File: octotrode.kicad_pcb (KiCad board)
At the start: 2 copper layers, 76 x 76 mm, 28 parts, among them J1 Conn_01x01, J2 Conn_01x01, J3 Conn_01x01, J4 Conn_01x01, J5 Conn_01x01, J6 Conn_01x01, Q1 Q_Photo_NPN, Q2 Q_Photo_NPN, Q3 Q_Photo_NPN, Q4 Q_Photo_NPN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

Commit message: add reverse voltage protection
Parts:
- added D5: D, Diode_SMD:D_SOD-123F, F.Cu at (188.5, 139.5)
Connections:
- J5 pad 1: +5V -> Net-(D5-Pad2)
- U1 pad 10: Net-(U1-Pad10) -> (no net)
- U1 pad 12: Net-(U1-Pad12) -> (no net)
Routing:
- net Net-(D5-Pad2): track 0.00 -> 10.4 mm

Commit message: correct LED orientation
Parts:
- moved D1 2.54 mm to (156.3, 146.0), turned to 180 degrees
- moved D3 2.54 mm to (163.7, 94.0), turned to 0 degrees
- moved D2 2.54 mm to (134.0, 116.3), turned to 90 degrees
- moved D4 2.54 mm to (186.0, 123.7), turned to 270 degrees
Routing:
- net Net-(D3-Pad2): track 3.43 -> 4.56 mm
- net Net-(D1-Pad2): track 3.43 -> 4.56 mm
- net Net-(D4-Pad2): track 3.43 -> 4.56 mm
- net Net-(D2-Pad2): track 3.43 -> 4.56 mm

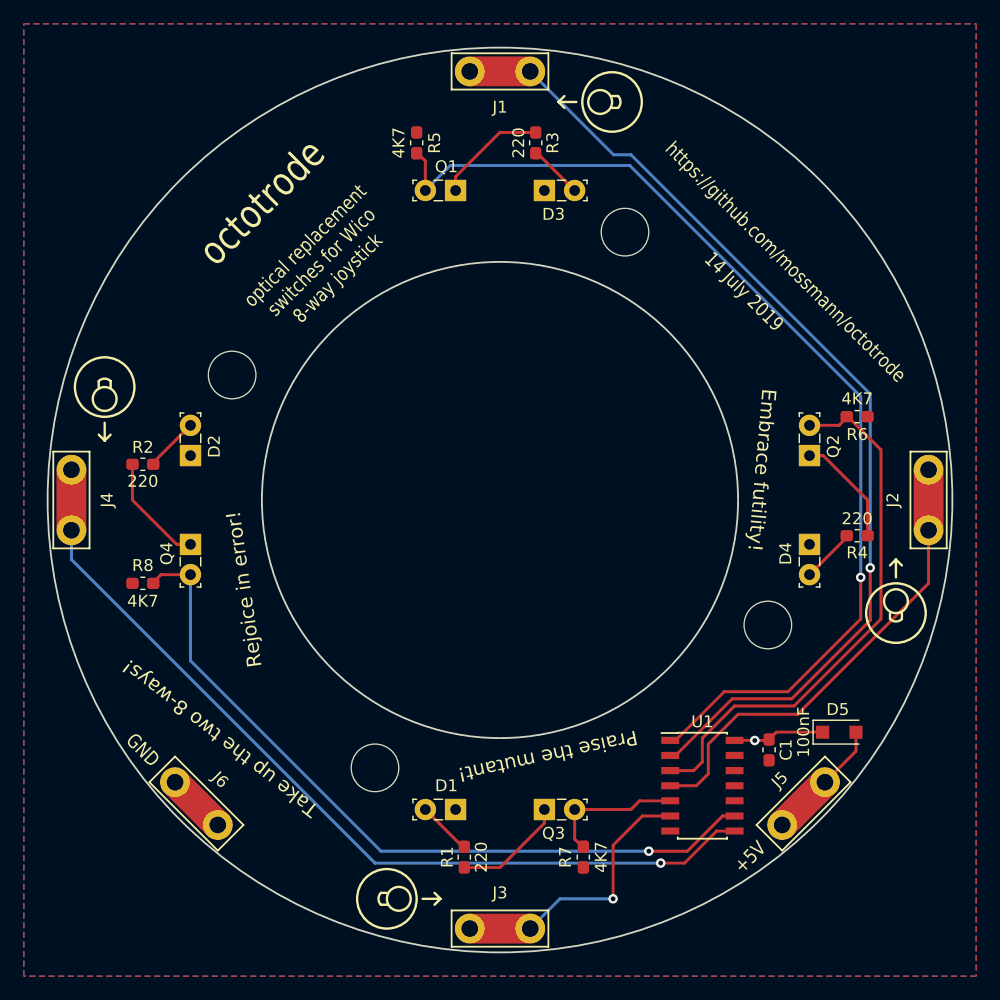
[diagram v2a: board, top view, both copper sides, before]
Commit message: widen optics position, shrink board
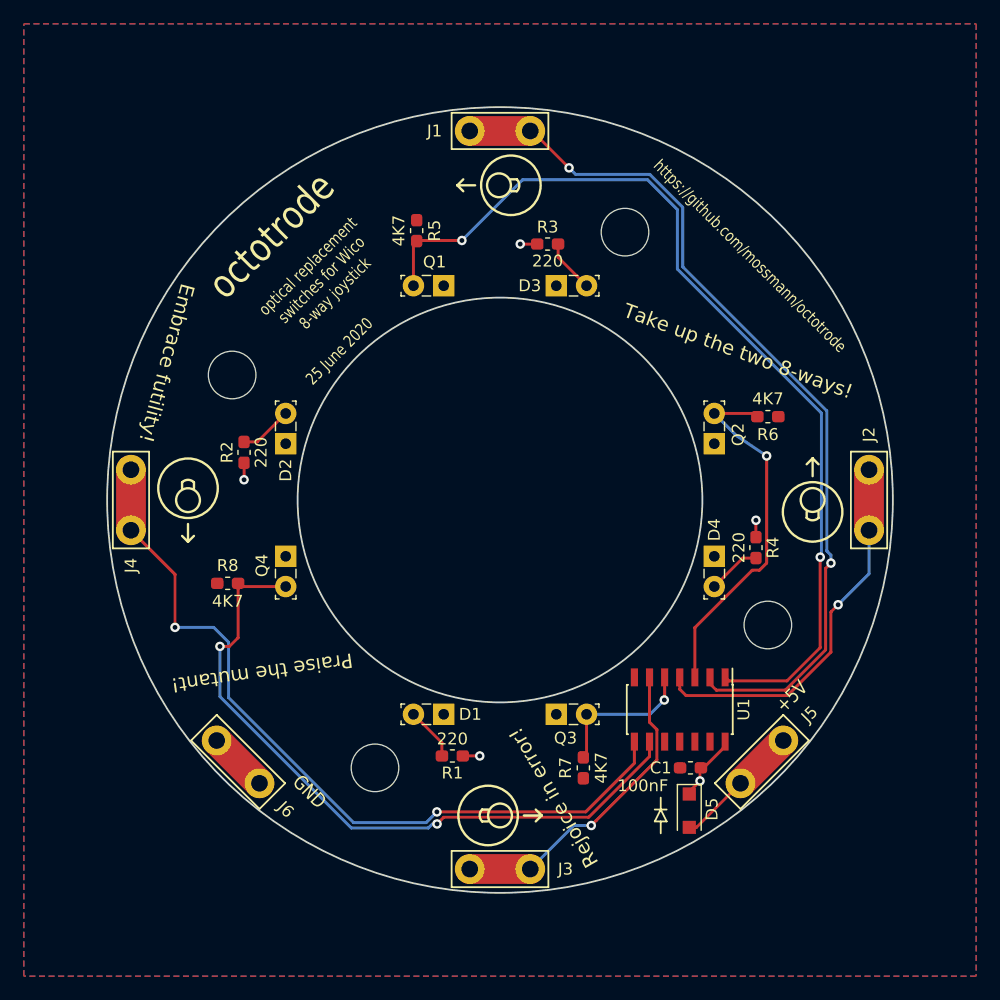
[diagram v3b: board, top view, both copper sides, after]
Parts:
- moved D5 14.2 mm to (175.9, 146.1), turned to 270 degrees
- moved R1 8.56 mm to (156.0, 141.5), turned to 180 degrees
- moved R2 8.56 mm to (138.5, 116.0), turned to 90 degrees
- moved R3 8.56 mm to (164.0, 98.5), turned to 0 degrees
- moved R4 8.56 mm to (181.5, 124.0), turned to 270 degrees
- moved D1 8.06 mm to (155.3, 138.0)
- moved D2 8.06 mm to (142.0, 115.3)
- moved D3 8.06 mm to (164.7, 102.0)
- moved D4 8.06 mm to (178.0, 124.7)
- moved Q1 8.06 mm to (155.3, 102.0)
- moved Q2 8.06 mm to (178.0, 115.3)
- moved Q3 8.06 mm to (164.7, 138.0)
- moved Q4 8.06 mm to (142.0, 124.7)
- moved R6 7.50 mm to (182.5, 113.0)
- moved R7 7.50 mm to (167.0, 142.5)
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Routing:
- net +5V: track 45.3 -> 11.5 mm, vias 1 -> 5
- net Net-(Q2-Pad2): track 45.8 -> 30.9 mm, vias 0 -> 1
- net Net-(J1-Pad1): track 85.4 -> 74.9 mm, vias 1 -> 2
- net Net-(J4-Pad1): track 74.9 -> 66.8 mm, vias 1 -> 2
- net Net-(Q1-Pad2): track 87.9 -> 80.1 mm, vias 1 -> 2
- net Net-(J2-Pad1): track 39.7 -> 32.1 mm, vias 0 -> 1
- net Net-(Q4-Pad2): track 64.3 -> 59.3 mm, vias 1 -> 2
- net Net-(J3-Pad1): track 23.4 -> 26.7 mm
- net Net-(Q3-Pad2): track 11.8 -> 12.7 mm, vias 0 -> 1
- net Net-(D5-Pad2): track 10.4 -> 10.9 mm
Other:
- board size 76 x 76 mm -> 66 x 66 mm
- rule pad_to_mask_clearance: 0.051 -> 0.0508
- board text added: "25 June 2020"
- board text removed: "14 July 2019"

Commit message: update license and bill of materials
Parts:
- added REF**: OSHW-Logo2_7.3x6mm_SilkScreen, Symbol:OSHW-Logo2_7.3x6mm_SilkScreen, F.Cu at (177.7, 101.5)
